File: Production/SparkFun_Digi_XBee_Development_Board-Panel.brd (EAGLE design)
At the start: 105.7 x 224.8 mm, 894 parts, among them J19 QWIIC_RIGHT_ANGLE, J27 QWIIC_RIGHT_ANGLE, J35 QWIIC_RIGHT_ANGLE, J4 QWIIC_RIGHT_ANGLE, J43 QWIIC_RIGHT_ANGLE, J7 QWIIC_RIGHT_ANGLE, Q1 3.1A/30V/105mΩ, Q2 3.1A/30V/105mΩ, Q3 3.1A/30V/105mΩ, Q4 3.1A/30V/105mΩ, Q5 3.1A/30V/105mΩ, Q6 3.1A/30V/105mΩ, U1 FSUSB30MUX_MSOP10, U10 ESD Diode, U11 FT231XS, U12 MCP73831, U13 FSUSB30MUX_MSOP10, U14 AP63203, U15 ESD Diode, U16 ESD Diode, U17 FT231XS, U18 MCP73831, U19 FSUSB30MUX_MSOP10, U2 AP63203, U20 AP63203, U21 ESD Diode, U22 ESD Diode, U23 FT231XS, U24 MCP73831, U25 FSUSB30MUX_MSOP10, U26 AP63203, U27 ESD Diode, U28 ESD Diode, U29 FT231XS, U3 ESD Diode, U30 MCP73831, U31 FSUSB30MUX_MSOP10, U32 AP63203, U33 ESD Diode, U34 ESD Diode, U35 FT231XS, U36 MCP73831, U4 MCP73831, U5 ESD Diode, U6 FSUSB30MUX_MSOP10, U7 FT231XS, U8 AP63203, U9 ESD Diode

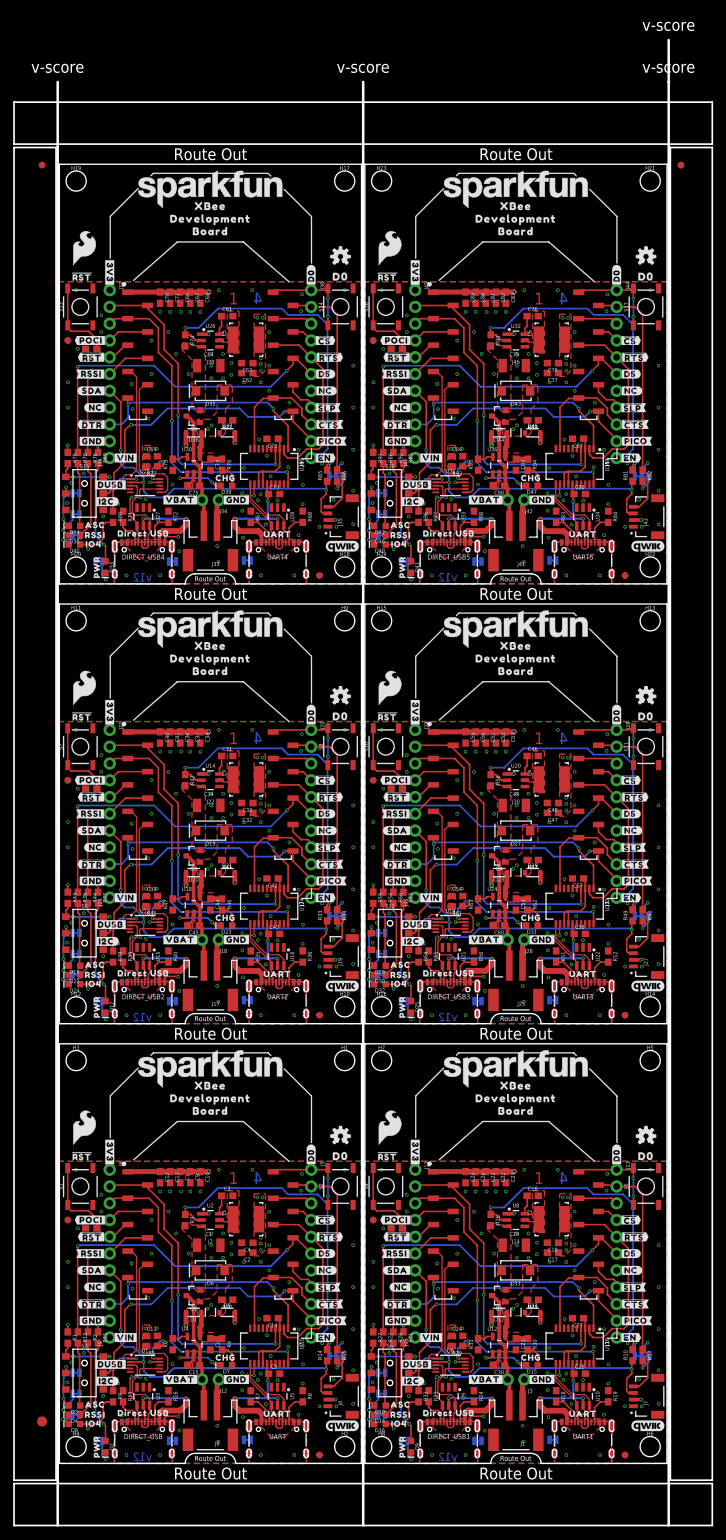
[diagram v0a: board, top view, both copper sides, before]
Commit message: Adds new panel - under new name unfortunately
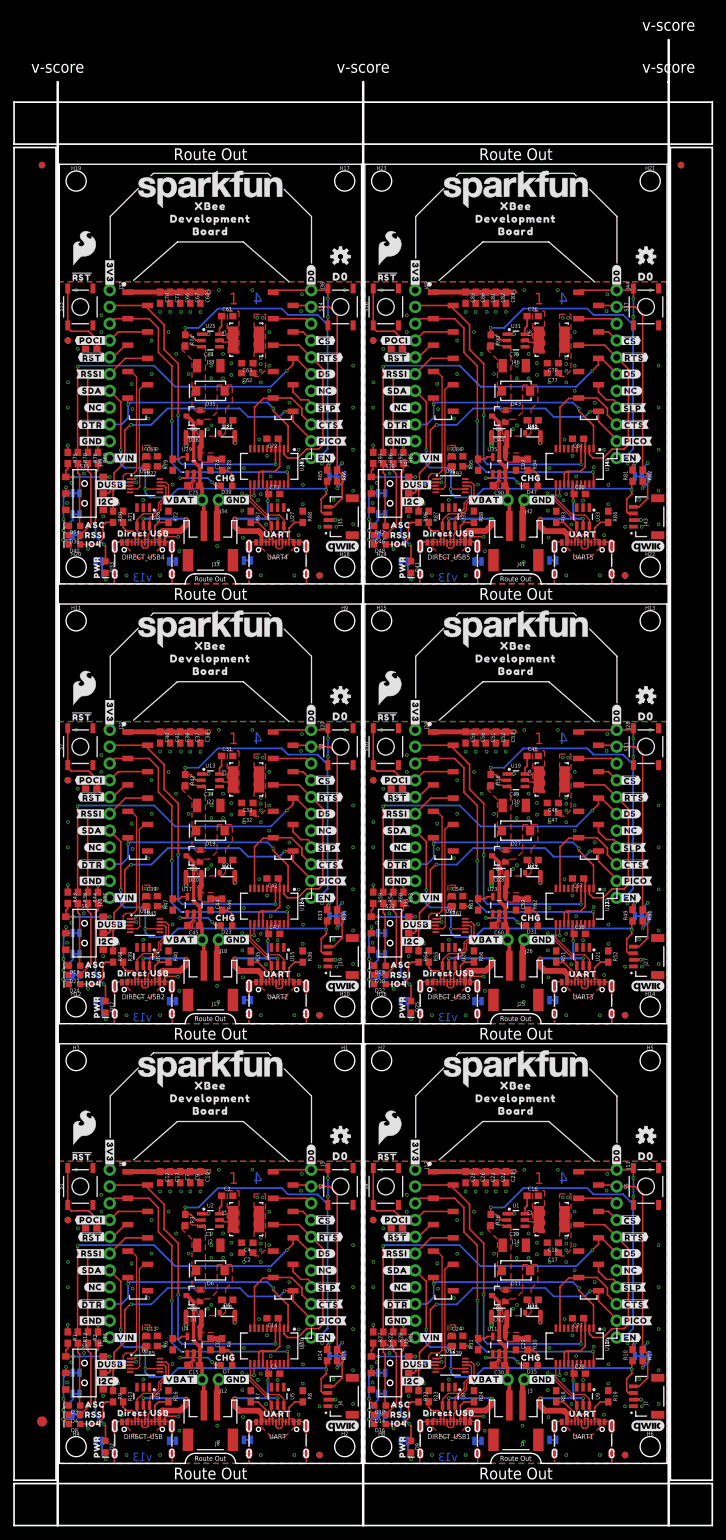
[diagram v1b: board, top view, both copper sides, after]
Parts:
- R29, R45, R5, R61, R77, R93: value 100 -> 0
- U1, U13, U19, U25, U31: value FSUSB30MUX_MSOP10 -> AP63203; device SparkFun-IC-Special-Function:MSOP10 -> SparkFun-IC-Power:SOT23-6
- U10, U16, U22, U28, U34: value ESD Diode -> FT231XS; device SparkFun-DiscreteSemi:SOT-23-6 -> SparkFun-IC-Comms:SSOP20_L
- U11, U17, U23, U29, U35: value FT231XS -> MCP73831; device SparkFun-IC-Comms:SSOP20_L -> SparkFun-IC-Power:SOT23-5
- U12, U18, U24, U30, U36: value MCP73831 -> FSUSB42MUX; device SparkFun-IC-Power:SOT23-5 -> SparkFun-IC-Special-Function:MSOP10
- U14, U20, U26, U32, U8: value AP63203 -> ESD Diode; device SparkFun-IC-Power:SOT23-6 -> SparkFun-DiscreteSemi:SOT-23-6
- U6: value FSUSB30MUX_MSOP10 -> FSUSB42MUX
- moved U1 60.3 mm to (69.1, 36.8), turned to 270 degrees
- moved U6 46.2 mm to (13.0, 14.9)
- moved U14 28.5 mm to (12.7, 76.7), turned to 180 degrees
- moved U20 28.5 mm to (58.9, 76.7), turned to 180 degrees
- moved U8 28.5 mm to (58.9, 10.2), turned to 180 degrees
- moved U26 28.5 mm to (12.7, 143.3), turned to 180 degrees
- moved U32 28.5 mm to (58.9, 143.3), turned to 180 degrees
- moved U13 24.1 mm to (22.9, 103.4), turned to 270 degrees
- moved U19 24.1 mm to (69.1, 103.4), turned to 270 degrees
- moved U25 24.1 mm to (22.9, 169.9), turned to 270 degrees
- moved U31 24.1 mm to (69.1, 169.9), turned to 270 degrees
- moved U21 20.3 mm to (79.2, 76.7)
- moved U33 20.3 mm to (79.2, 143.3)
- moved U9 20.3 mm to (79.2, 10.2)
- moved U15 20.3 mm to (33.0, 76.7)
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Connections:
- net 3.3V1: now also U1.1; no longer U8.1
- net 3.3V2: now also U13.1; no longer U14.1
- net 3.3V3: now also U19.1; no longer U20.1
- net 3.3V4: now also U25.1; no longer U26.1
- net 3.3V5: now also U31.1; no longer U32.1
- net D+1: now also U10.11, U9.6; no longer U10.6, U11.11
- net D+2: now also U15.6, U16.11; no longer U16.6, U17.11
- net D+3: now also U21.6, U22.11; no longer U22.6, U23.11
- net D+4: now also U27.6, U28.11; no longer U28.6, U29.11
- net D+5: now also U33.6, U34.11; no longer U34.6, U35.11
- net D-1: now also U10.12, U9.4; no longer U10.4, U11.12
- net D-2: now also U15.4, U16.12; no longer U16.4, U17.12
- net D-3: now also U21.4, U22.12; no longer U22.4, U23.12
- net D-4: now also U27.4, U28.12; no longer U28.4, U29.12
- net D-5: now also U33.4, U34.12; no longer U34.4, U35.12
- net D11/SDA: now also U6.7; no longer U1.2
- net D11/SDA1: now also U12.7; no longer U6.2
- net D11/SDA2: now also U18.7; no longer U13.2
- net D11/SDA3: now also U24.7; no longer U19.2
- net D11/SDA4: now also U30.7; no longer U25.2
- net D11/SDA5: now also U36.7; no longer U31.2
- net D13/TXO1: now also U10.4; no longer U11.4
- net D13/TXO2: now also U16.4; no longer U17.4
- net D13/TXO3: now also U22.4; no longer U23.4
- net D13/TXO4: now also U28.4; no longer U29.4
- net D13/TXO5: now also U34.4; no longer U35.4
- net D14/RXI1: now also U10.20; no longer U11.20
- net D14/RXI2: now also U16.20; no longer U17.20
- net D14/RXI3: now also U22.20; no longer U23.20
- net D14/RXI4: now also U28.20; no longer U29.20
- net D14/RXI5: now also U34.20; no longer U35.20
- net D6/!RTS!1: now also U10.2; no longer U11.2
- net D6/!RTS!2: now also U16.2; no longer U17.2
- net D6/!RTS!3: now also U22.2; no longer U23.2
- net D6/!RTS!4: now also U28.2; no longer U29.2
- net D6/!RTS!5: now also U34.2; no longer U35.2
- net D7/!CTS!1: now also U10.9; no longer U11.9
- net D7/!CTS!2: now also U16.9; no longer U17.9
- net D7/!CTS!3: now also U22.9; no longer U23.9
- net D7/!CTS!4: now also U28.9; no longer U29.9
- net D7/!CTS!5: now also U34.9; no longer U35.9
- net D8/!DTR!1: now also U10.1; no longer U11.1
- net D8/!DTR!2: now also U16.1; no longer U17.1
- net D8/!DTR!3: now also U22.1; no longer U23.1
- net D8/!DTR!4: now also U28.1; no longer U29.1
- net D8/!DTR!5: now also U34.1; no longer U35.1
- net DIRECT_D+: now also U6.9; no longer U1.3
- net DIRECT_D+1: now also U12.9, U8.6; no longer U6.3, U9.6
- net DIRECT_D+2: now also U14.6, U18.9; no longer U13.3, U15.6
- net DIRECT_D+3: now also U20.6, U24.9; no longer U19.3, U21.6
- net DIRECT_D+4: now also U26.6, U30.9; no longer U25.3, U27.6
- net DIRECT_D+5: now also U32.6, U36.9; no longer U31.3, U33.6
- net DIRECT_D-: now also U6.8; no longer U1.7
- net DIRECT_D-1: now also U12.8, U8.4; no longer U6.7, U9.4
- net DIRECT_D-2: now also U14.4, U18.8; no longer U13.7, U15.4
- net DIRECT_D-3: now also U20.4, U24.8; no longer U19.7, U21.4
- net DIRECT_D-4: now also U26.4, U30.8; no longer U25.7, U27.4
- net DIRECT_D-5: now also U32.4, U36.8; no longer U31.7, U33.4
- net DIRECT_SELECT: now also U6.2; no longer U1.1
- net DIRECT_SELECT1: now also U12.2; no longer U6.1
- net DIRECT_SELECT2: now also U18.2; no longer U13.1
- net DIRECT_SELECT3: now also U24.2; no longer U19.1
- net DIRECT_SELECT4: now also U30.2; no longer U25.1
- net DIRECT_SELECT5: now also U36.2; no longer U31.1
- net EN1: now also U1.2; no longer U8.2
- net EN2: now also U13.2; no longer U14.2
- net EN3: now also U19.2; no longer U20.2
- net EN4: now also U25.2; no longer U26.2
- net EN5: now also U31.2; no longer U32.2
- net GND: now also U6.10, U6.5; no longer U1.5, U1.9
- net GND1: now also U1.4, U10.16, U10.6, U11.2, U12.10, U12.5, U8.2; no longer U10.2, U11.16, U11.6, U12.2, U6.5, U6.9, U8.4
- net GND2: now also U13.4, U14.2, U16.16, U16.6, U17.2, U18.10, U18.5; no longer U13.5, U13.9, U14.4, U16.2, U17.16, U17.6, U18.2
- net GND3: now also U19.4, U20.2, U22.16, U22.6, U23.2, U24.10, U24.5; no longer U19.5, U19.9, U20.4, U22.2, U23.16, U23.6, U24.2
- net GND4: now also U25.4, U26.2, U28.16, U28.6, U29.2, U30.10, U30.5; no longer U25.5, U25.9, U26.4, U28.2, U29.16, U29.6, U30.2
- net GND5: now also U31.4, U32.2, U34.16, U34.6, U35.2, U36.10, U36.5; no longer U31.5, U31.9, U32.4, U34.2, U35.16, U35.6, U36.2
- net N$100: now also U31.6; no longer U32.6
- net N$101: now also U31.5; no longer U32.5
- net N$103: now also U36.1; no longer U31.10
- net N$104: now also U35.5; no longer U36.5
- net N$105: now also U35.1; no longer U36.1
- net N$108: now also U34.13, U34.14, U34.3; no longer U35.13, U35.14, U35.3
- net N$27: now also U1.3; no longer U8.3
- net N$28: now also U1.6; no longer U8.6
- net N$29: now also U1.5; no longer U8.5
- net N$3: now also U6.1; no longer U1.10
- net N$31: now also U12.1; no longer U6.10
- net N$32: now also U11.5; no longer U12.5
- net N$33: now also U11.1; no longer U12.1
- net N$36: now also U10.13, U10.14, U10.3; no longer U11.13, U11.14, U11.3
- net N$45: now also U13.3; no longer U14.3
- net N$46: now also U13.6; no longer U14.6
- net N$47: now also U13.5; no longer U14.5
- net N$49: now also U18.1; no longer U13.10
- net N$50: now also U17.5; no longer U18.5
- net N$51: now also U17.1; no longer U18.1
- net N$54: now also U16.13, U16.14, U16.3; no longer U17.13, U17.14, U17.3
- net N$63: now also U19.3; no longer U20.3
- net N$64: now also U19.6; no longer U20.6
- net N$65: now also U19.5; no longer U20.5
- net N$67: now also U24.1; no longer U19.10
- net N$68: now also U23.5; no longer U24.5
- net N$69: now also U23.1; no longer U24.1
- net N$72: now also U22.13, U22.14, U22.3; no longer U23.13, U23.14, U23.3
- net N$81: now also U25.3; no longer U26.3
- net N$82: now also U25.6; no longer U26.6
- net N$83: now also U25.5; no longer U26.5
- net N$85: now also U30.1; no longer U25.10
- net N$86: now also U29.5; no longer U30.5
- net N$87: now also U29.1; no longer U30.1
- net N$90: now also U28.13, U28.14, U28.3; no longer U29.13, U29.14, U29.3
- net N$99: now also U31.3; no longer U32.3
- net VIN1: now also U11.4; no longer U12.4
- net VIN2: now also U17.4; no longer U18.4
- net VIN3: now also U23.4; no longer U24.4
- net VIN4: now also U29.4; no longer U30.4
- net VIN5: now also U35.4; no longer U36.4
- net V_BATT1: now also U11.3; no longer U12.3
- net V_BATT2: now also U17.3; no longer U18.3
- net V_BATT3: now also U23.3; no longer U24.3
- net V_BATT4: now also U29.3; no longer U30.3
- net V_BATT5: now also U35.3; no longer U36.3
- net V_USB1: now also U10.15, U9.5; no longer U10.5, U11.15
- net V_USB2: now also U15.5, U16.15; no longer U16.5, U17.15
- net V_USB3: now also U21.5, U22.15; no longer U22.5, U23.15
- net V_USB4: now also U27.5, U28.15; no longer U28.5, U29.15
- net V_USB5: now also U33.5, U34.15; no longer U34.5, U35.15
- net V_USB_1: now also U8.5; no longer U9.5
- net V_USB_3: now also U14.5; no longer U15.5
- net V_USB_4: now also U20.5; no longer U21.5
- net V_USB_5: now also U26.5; no longer U27.5
- net V_USB_6: now also U32.5; no longer U33.5
- net XBEE_D+/SDA: now also U6.3; no longer U1.4
- net XBEE_D+/SDA1: now also U12.3; no longer U6.4
- net XBEE_D+/SDA2: now also U18.3; no longer U13.4
- net XBEE_D+/SDA3: now also U24.3; no longer U19.4
- net XBEE_D+/SDA4: now also U30.3; no longer U25.4
- net XBEE_D+/SDA5: now also U36.3; no longer U31.4
- net XBEE_D-: now also U6.4; no longer U1.6
- net XBEE_D-1: now also U12.4; no longer U6.6
- net XBEE_D-2: now also U18.4; no longer U13.6
- net XBEE_D-3: now also U24.4; no longer U19.6
- net XBEE_D-4: now also U30.4; no longer U25.6
- net XBEE_D-5: now also U36.4; no longer U31.6
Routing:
- net XBEE_D-3: track 21.7 -> 17.9 mm
- net XBEE_D-: track 21.7 -> 17.9 mm
- net XBEE_D-2: track 21.7 -> 17.9 mm
- net XBEE_D-1: track 21.7 -> 17.9 mm
- net XBEE_D-5: track 21.7 -> 17.9 mm
- net XBEE_D-4: track 21.7 -> 17.9 mm
- net GND3: track 10.4 -> 8.95 mm, vias 78 -> 77
- net GND2: track 10.4 -> 8.95 mm, vias 78 -> 77
- net GND: track 10.4 -> 8.95 mm, vias 78 -> 77
- net GND1: track 10.4 -> 8.95 mm, vias 78 -> 77
- net GND5: track 10.4 -> 8.95 mm, vias 78 -> 77
- net GND4: track 10.4 -> 8.95 mm, vias 78 -> 77
- net N$103: track 6.17 -> 7.47 mm
- net N$85: track 6.17 -> 7.47 mm
- net N$67: track 6.17 -> 7.47 mm
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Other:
- board text added: "v13"
- board text removed: "v12"
